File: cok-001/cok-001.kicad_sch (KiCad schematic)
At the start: 282 parts, among them J2501 HDMI_A, J3209 ATA Power, J3221 ATA0 for BD, J3301 USB_A_Stacked, J3302 USB_A_Stacked, J3401 Conn_01x22_Pin, J4001 Conn_01x03_Pin, J4003 Conn_01x02_Pin, J4009 Conn_01x30_Socket, J4010 Conn_01x10_Socket, Q2401 DTC144E, Q2402 SI2303BDS, Q4014 DTC143ZUA, U1101 ADT7461A0002RMZR, U1201 Y0_XDR0, U1202 Y0_XDR1, U1301 Y1_XDR0, U1302 Y1_XDR1, U2101 ADT7461A0002RMZR, U2105 TC7WP3125FK, U2108 ICS651MLFT, U2402 L7809, U2403 L7805, U2407 MM1593DFBEG, U3302 BU9869W, U3802 K9F1G08U0A, U3803 K9F1G08U0A, U6005 NCP511SN33T1G, U6006 NCP511SN18T1, U6008 NCP511SN18T1, U6009 NCP511SN33T1G, U6011 NCP511SN18T1, U6019 NCP511SN18T1, U7301 CXD9208GP, Y2101 24.576MHz, Y4001 Crystal, Y4002 Crystal

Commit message: sheets
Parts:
- removed C1103: 0.001u 50V, Capacitor_SMD:C_0402_1005Metric, symbol Device:C
- removed C1104, C1313, C1314, C1315, C1316, C1317, C1318, C1319, C1320, C1321, C1322, C1323, C1324, C1325, C1326, C1327, C1328, C1329, C1330, C1331, C1332, C1333, C1334, C1335, C1336, C1337, C1338, C1339, C1340, C1341, C1342: 0.1u 10V, Capacitor_SMD:C_0402_1005Metric, symbol Device:C
- removed R1106, R1107: 100, Resistor_SMD:R_0402_1005Metric, symbol Device:R_US
- removed U1101: ADT7461A0002RMZR, Package_SO:MSOP-8_3x3mm_P0.65mm, symbol PS3:ADT7461A
- removed U1201: Y0_XDR0, PS3:FBGA-104_16x11_15.18x14.56mm, symbol PS3:XDR_DRAM
- removed U1202: Y0_XDR1, PS3:FBGA-104_16x11_15.18x14.56mm, symbol PS3:XDR_DRAM
- removed U1301: Y1_XDR0, PS3:FBGA-104_16x11_15.18x14.56mm, symbol PS3:XDR_DRAM
- removed U1302: Y1_XDR1, PS3:FBGA-104_16x11_15.18x14.56mm, symbol PS3:XDR_DRAM
- added C2272: 100p, Capacitor_SMD:C_0402_1005Metric, symbol Device:C
- added C3314: 0.1u, Capacitor_SMD:C_0402_1005Metric, symbol Device:C
- added C3412, C3413, C3414, C3415: 0.01u, Capacitor_SMD:C_0402_1005Metric, symbol Device:C
- added D251, D252, D253, D254, D255, D256, D257, D258: ESD5Zxx, Diode_SMD:D_SOD-923, symbol Diode:ESD5Zxx
- added L2501, L2502, L2503, L2504, L3301, L3302, L3401, L3402: L_Iron_Coupled_Small, Inductor_SMD:L_CommonModeChoke_Coilcraft_0805USB, symbol Device:L_Iron_Coupled_Small_1243
- added R2106: 10k, Resistor_SMD:R_0402_1005Metric, symbol Device:R_US
- added R3328, R3329: 0, Resistor_SMD:R_0603_1608Metric, symbol Device:R_US
- added R3360, R3361, R3362, R3363, R3364, R3365, R3366, R3367: 0, Resistor_SMD:R_0402_1005Metric, symbol Device:R_US
- added TP9505, TP9506, TP9507, TP9508, TP9509, TP9510, TP9511, TP9512, TP9520, TP9522, TP9527, TP9529: TestPoint, TestPoint:TestPoint_Pad_1.0x1.0mm, symbol Connector:TestPoint
- added U3303: ~, Package_SO:SOIC-8_3.9x4.9mm_P1.27mm, symbol PS3:BD6517F
- added U3401: ~, Package_QFP:LQFP-64_10x10mm_P0.5mm, symbol PS3:88SA8040C0
- TP40005, TP4001, TP4002, TP4003, TP4004, TP4005, TP4006, TP4007, TP4008, TP4009, TP4016, TP4020, TP4021, TP4022, TP4034, TP4035, TP4036, TP4040, TP4044, TP4046, TP4075, TP4080, TP4081, TP4082, TP4083, TP4089, TP4090, TP4093, TP4096, TP4097, TP4105, TP9401, TP9402: footprint (none) -> TestPoint:TestPoint_Pad_1.0x1.0mm
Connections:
- net GND: now also U3305.1 (AGND), U3305.12 (ANGD), U3305.19 (AGND), U3305.23 (AGND), U3305.29 (AGND), C2272.2, C3314.2, D251.2 (A), D252.2 (A), D253.2 (A), D254.2 (A), D255.2 (A), D256.2 (A), D257.2 (A), D258.2 (A), U3303.6 (GND), U3401.42 (GND), U3401.57 (GND), U3401.8 (GND); no longer U2502.C1 (GND), U2502.C2
- net SW_AVCG: now also U2102.12 (OE), C2272.1, R2106.2
- net at U2102.6 (Vdd54): now also R2106.1
- net at J2501.1 (D2+): now also L2501.3
- net at J2501.10 (CK+): now also L2504.3
- net at J2501.12 (CK-): now also L2504.2
- net at J2501.19 (HPD): now also U2502.A1 (HPD)
- net at J2501.3 (D2-): now also L2501.2
- net at J2501.4 (D1+): now also L2502.3
- net at J2501.6 (D1-): now also L2502.2
- net at J2501.7 (D0+): now also L2503.3
- net at J2501.9 (D0-): now also L2503.2
- net at U4002.B16 (OSCOUT): now also C4028.1, Y4002.2
- net at U4002.C16 (OSCIN): now also C4027.1, Y4002.1
- net at J3302.1 (VBUS1): now also U3304.5 (OUTB), TP9522.1
- net at J3302.2 (D1-): now also L3301.4, TP9512.1
- net at J3302.3 (D1+): now also L3301.1, TP9511.1
- net at J3302.5 (VBUS2): now also U3304.8 (OUTA), TP9529.1
- net at J3302.6 (D2-): now also L3302.4, TP9510.1
- net at J3302.7 (D2+): now also L3302.1, TP9509.1
- net at U2502.A10 (TXC+_25): now also D252.1 (K), L2504.4
- net at U2502.A11 (TXC-_25): now also D251.1 (K), L2504.1
- net at U2502.A2 (TX2+_25): now also D258.1 (K), L2501.4
- net at U2502.A3 (TX2-_25): now also D257.1 (K), L2501.1
- net at U2502.A5 (TX1+_25): now also D256.1 (K), L2502.4
- net at U2502.A6 (TX1-_25): now also D255.1 (K), L2502.1
- net at U2502.A7 (TX0+_25): now also D254.1 (K), L2503.4
- net at U2502.A8 (TX0-_25): now also D253.1 (K), L2503.1
- net at U3305.14 (DM2): now also R3362.1
- net at U3305.15 (DP2): now also R3363.1
- net at U3305.25 (DM3): now also R3365.2
- net at U3305.26 (DP3): now also R3364.2
- net at U3305.3 (DM0): now also R3328.1
- net at U3305.31 (DM4): now also R3367.2
- net at U3305.32 (DP4): now also R3366.2
- net at U3305.4 (DP0): now also R3329.1
- net at U3305.8 (DM1): now also R3360.1
- net at U3305.9 (DP1): now also R3361.1
- net at J3301.1 (VBUS1): now also TP9520.1, U3303.5 (OUTB)
- net at J3301.2 (D1-): now also TP9508.1
- net at J3301.3 (D1+): now also TP9507.1
- net at J3301.5 (VBUS2): now also TP9527.1, U3303.8 (OUTA)
- net at J3301.6 (D2-): now also TP9506.1
- net at J3301.7 (D2+): now also TP9505.1
- net at J3401.S2 (A+): now also L3401.4
- net at J3401.S3 (A-): now also L3401.1
- net at J3401.S5 (B-): now also L3402.4
- net at J3401.S6 (B+): now also L3402.1
- new net: L3301.2, R3366.1
- new net: L3301.3, R3367.1
- new net: C3415.1, U3401.27 (RX_P)
- new net: C3415.2, L3402.2
- new net: C3413.1, U3401.28 (RX_M)
- new net: C3414.1, U3401.31 (TX_M)
- new net: C3412.1, U3401.32 (TX_P)
- new net: L3302.3, R3365.1
- new net: C3314.1, U3303.7 (VDD)
- new net: C3414.2, L3401.2
- new net: C3412.2, L3401.3
- new net: C3413.2, L3402.3
- new net: L3302.2, R3364.1
- new net SB_USB1_DM: R3328.2
- new net SB_USB1_DP: R3329.2
- no-connect marks 30 -> 37
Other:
- added sheet Resistors, Bypassing (resistors.kicad_sch)
- added sheet XDR DRAM (xdram.kicad_sch)
- moved on the sheet: C2101, C2102, C2451, C3246, C3247, C3301, C3309, C3311, C3313, C3316, C3328, C6116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

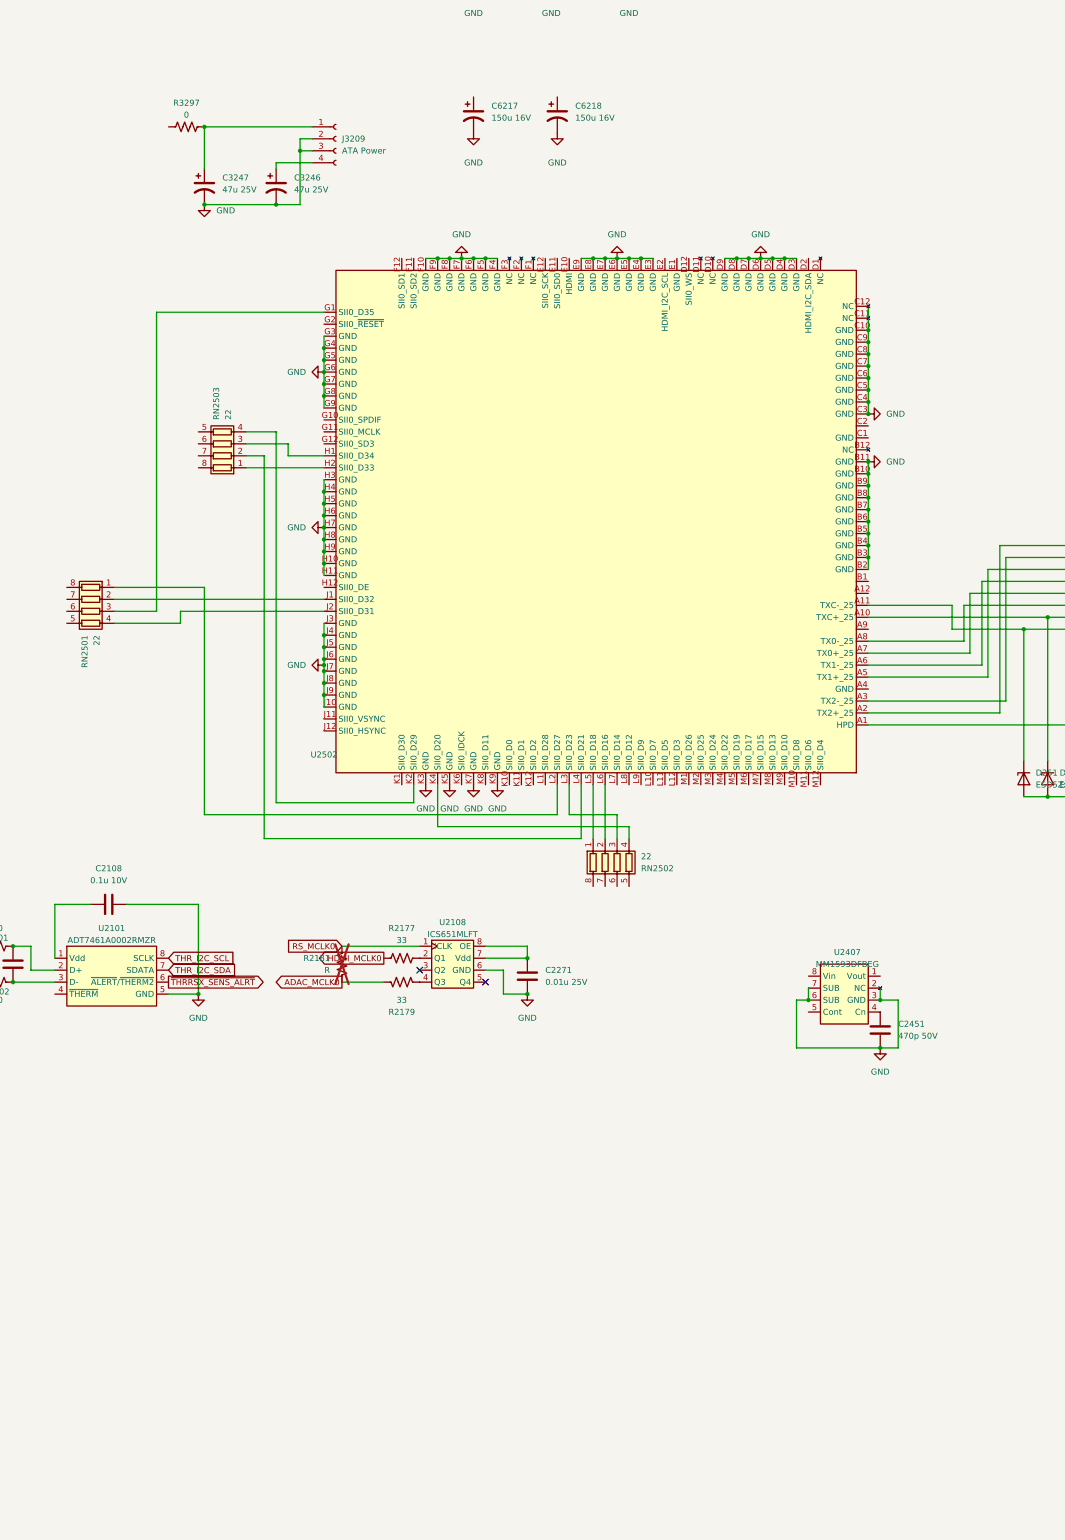
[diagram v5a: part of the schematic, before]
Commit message: fix Sil9132 symbol
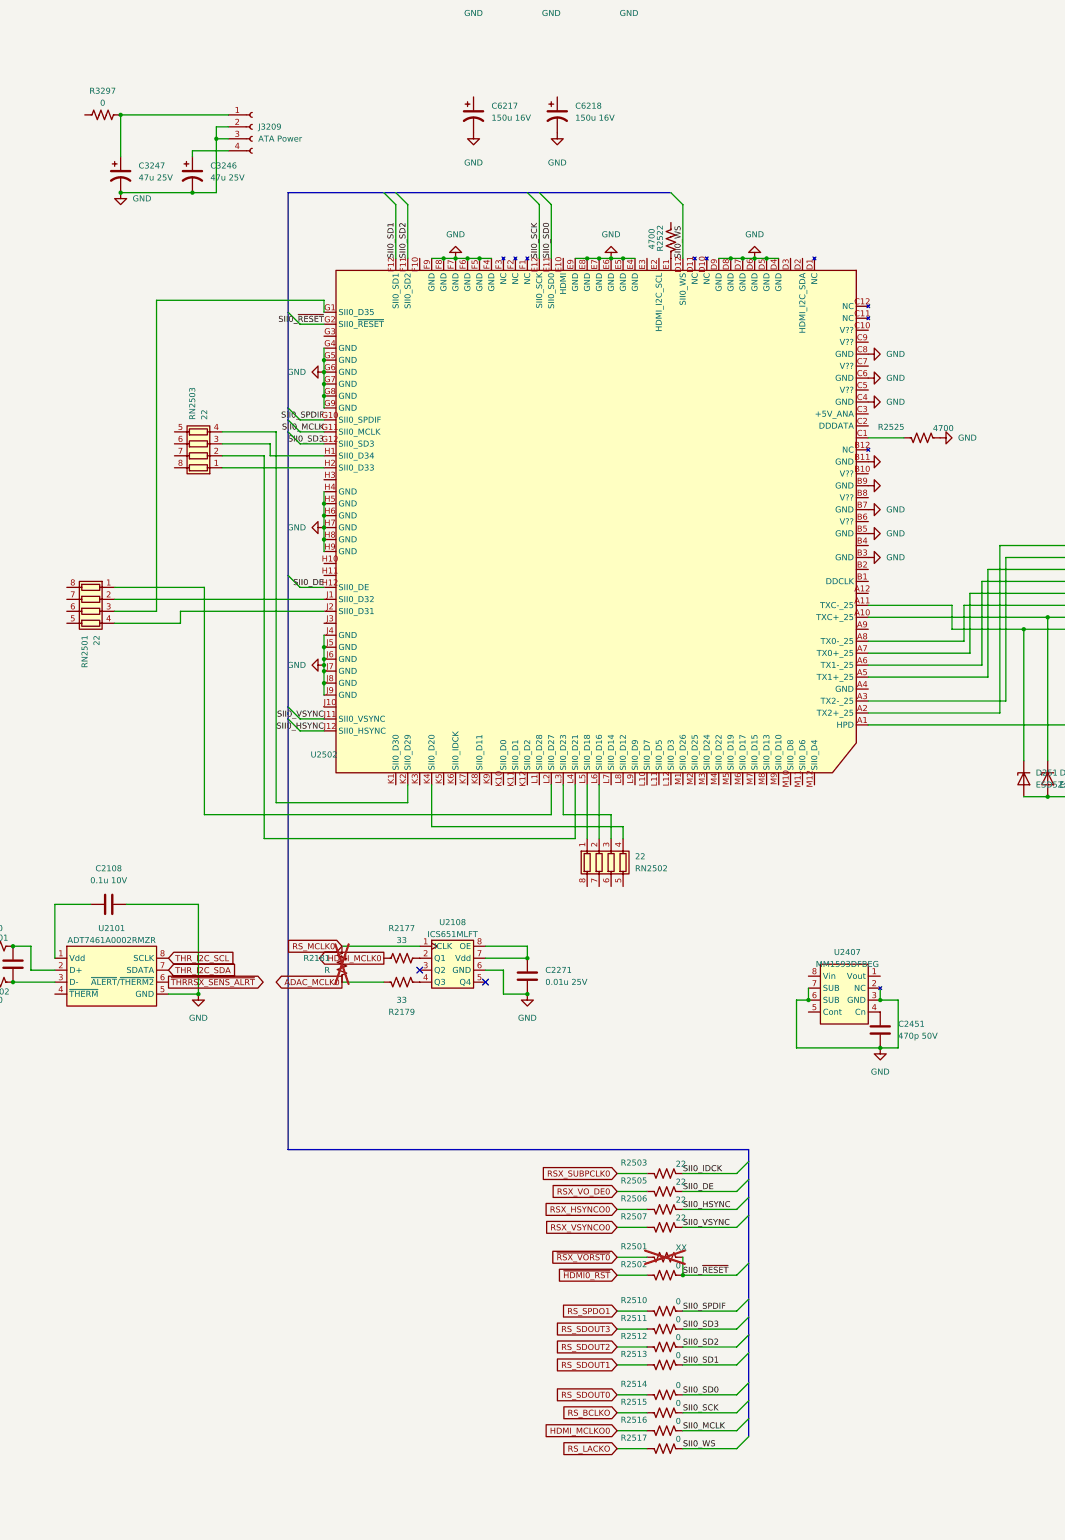
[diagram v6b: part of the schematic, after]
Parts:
- added R2501: XX, Resistor_SMD:R_0402_1005Metric, symbol Device:R_US
- added R2502, R2510, R2511, R2512, R2513, R2514, R2515, R2516, R2517: 0, Resistor_SMD:R_0402_1005Metric, symbol Device:R_US
- added R2503, R2505, R2506, R2507: 22, Resistor_SMD:R_0402_1005Metric, symbol Device:R_US
- added R2522, R2525: 4700, Resistor_SMD:R_0402_1005Metric, symbol Device:R_US
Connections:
- net GND: now also R2525.2; no longer U2502.B10 (GND), U2502.B2 (GND), U2502.B4 (GND), U2502.B6 (GND), U2502.B8 (GND), U2502.C10 (GND), U2502.C12 (NC), U2502.C3 (GND), U2502.C5 (GND), U2502.C7 (GND), U2502.C9 (GND), U2502.D3 (GND), U2502.E3 (GND), U2502.F10 (GND), U2502.G3 (GND), U2502.H10 (GND), U2502.H11 (GND), U2502.H3 (GND), U2502.J10 (GND), U2502.J3 (GND), U2502.K3 (GND), U2502.K5 (GND), U2502.K7 (GND), U2502.K9 (GND)
- net ~{HDMI0_RST}: now also R2502.1
- net at U4002.B16 (OSCOUT): now also C4028.1, Y4002.2
- net at U4002.C16 (OSCIN): now also C4027.1, Y4002.1
- net at U2502.C1: now also R2525.1
- net SII0_WS: now reaches U2502.D12 (SII0_WS)
- net SII0_WS: now also R2517.2
- net at U2502.E1: now also R2522.2
- net SII0_SD0: now reaches U2502.E11 (SII0_SD0)
- net SII0_SD0: now also R2514.2
- net SII0_SCK: now reaches U2502.E12 (SII0_SCK)
- net SII0_SCK: now also R2515.2
- net SII0_SD2: now reaches U2502.F11 (SII0_SD2)
- net SII0_SD2: now also R2512.2
- net SII0_SD1: now reaches U2502.F12 (SII0_SD1)
- net SII0_SD1: now also R2513.2
- net SII0_SPDIF: now reaches U2502.G10 (SII0_SPDIF)
- net SII0_SPDIF: now also R2510.2
- net SII0_MCLK: now reaches U2502.G11 (SII0_MCLK)
- net SII0_MCLK: now also R2516.2
- net SII0_SD3: now reaches U2502.G12 (SII0_SD3)
- net SII0_SD3: now also R2511.2
- net SII0_~{RESET}: now reaches U2502.G2 (SII0_~{RESET})
- net SII0_~{RESET}: now also R2501.2, R2502.2
- net SII0_DE: now reaches U2502.H12 (SII0_DE)
- net SII0_DE: now also R2505.2
- net SII0_VSYNC: now reaches U2502.J11 (SII0_VSYNC)
- net SII0_VSYNC: now also R2507.2
- net SII0_HSYNC: now reaches U2502.J12 (SII0_HSYNC)
- net SII0_HSYNC: now also R2506.2
- new net HDMI_MCLKO0: R2516.1
- new net RSX_HSYNCO0: R2506.1
- new net RSX_SUBPCLK0: R2503.1
- new net RSX_VO_DE0: R2505.1
- new net RSX_VSYNCO0: R2507.1
- new net RS_BCLKO: R2515.1
- new net RS_LACKO: R2517.1
- new net RS_SDOUT0: R2514.1
- new net RS_SDOUT1: R2513.1
- new net RS_SDOUT2: R2512.1
- new net RS_SDOUT3: R2511.1
- new net RS_SPDO1: R2510.1
- new net SII0_IDCK: R2503.2
- new net ~{RSX_VORST0}: R2501.1
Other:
- moved on the sheet: C3246, C3247, J3209, R3297, RN2502, RN2503

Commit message: added hdmi and jtag
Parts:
- removed D251, D252, D253, D254, D255, D256, D257, D258: ESD5Zxx, Diode_SMD:D_SOD-923, symbol Diode:ESD5Zxx
- removed J2501: HDMI_A, Connector_FFC-FPC:Hirose_FH12-19S-0.5SH_1x19-1MP_P0.50mm_Horizontal, symbol Connector:HDMI_A
- removed L2501, L2502, L2503, L2504: L_Iron_Coupled_Small, Inductor_SMD:L_CommonModeChoke_Coilcraft_0805USB, symbol Device:L_Iron_Coupled_Small_1243
- removed R2501: XX, Resistor_SMD:R_0402_1005Metric, symbol Device:R_US
- removed R2502, R2510, R2511, R2512, R2513, R2514, R2515, R2516, R2517: 0, Resistor_SMD:R_0402_1005Metric, symbol Device:R_US
- removed R2503, R2505, R2506, R2507: 22, Resistor_SMD:R_0402_1005Metric, symbol Device:R_US
- removed R2522, R2525: 4700, Resistor_SMD:R_0402_1005Metric, symbol Device:R_US
- removed RN2501, RN2502, RN2503: 22, Resistor_SMD:R_Array_Convex_4x0402, symbol Device:R_Pack04
- removed U2502: ~, Package_BGA:BGA-144_13.0x13.0mm_Layout12x12_P1.0mm, symbol PS3:Sil9132
- added H1, H2, H3, H4, H5, H6: MountingHole_Pad, MountingHole:MountingHole_4.3mm_M4_DIN965_Pad, symbol Mechanical:MountingHole_Pad
- D4007, D4008, D4009: footprint (none) -> Diode_SMD:D_SOD-923
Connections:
- net GND: now also H1.1, H2.1, H3.1, H4.1, H5.1, H6.1
- net at U4002.B16 (OSCOUT): now also C4028.1, Y4002.2
- net at U4002.C16 (OSCIN): now also C4027.1, Y4002.1
- no-connect marks 37 -> 35
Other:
- added sheet HDMI out (hdmi.kicad_sch)
- moved on the sheet: C2103, C2108, C2271, C2451, C3246, C3247, C6217, C6218, J3209, R2101, R2102, R2177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

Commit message: sif
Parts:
- removed C3823, C3824, C3825, C3826: 0.1u, Capacitor_SMD:C_0402_1005Metric, symbol Device:C
- removed C7347, C7348, C7349, C7350: 0.01u, Capacitor_SMD:C_0402_1005Metric, symbol Device:C
- removed C7354: 100p, Capacitor_SMD:C_0402_1005Metric, symbol Device:C
- removed R1, R7312, R7313: 56, Resistor_SMD:R_0402_1005Metric, symbol Device:R_US
- removed R3812, R3813, R3814, R3815: 0, Resistor_SMD:R_0402_1005Metric, symbol Device:R_US
- removed R3830, R3831, R3832, R3833, R3834, R3835, R3836, R3837: 10k, Resistor_SMD:R_0402_1005Metric, symbol Device:R_US
- removed R3840, R3841: 2200, Resistor_SMD:R_0402_1005Metric, symbol Device:R_US
- removed R7302, R7303, R7304, R7305, R7306, R7307, R7308, R7309: 4700, Resistor_SMD:R_0402_1005Metric, symbol Device:R_US
- removed R7314: 22, Resistor_SMD:R_0402_1005Metric, symbol Device:R_US
- removed RN7301, RN7302, RN7303, RN7304, RN7306, RN7307, RN7308, RN7309, RN7311: 56, Resistor_SMD:R_Array_Convex_4x0402, symbol Device:R_Pack04
- removed TP7301, TP7302, TP7303, TP7304, TP7305, TP7306, TP7307, TP7308, TP7309, TP7310, TP7311: TestPoint, TestPoint:TestPoint_Pad_1.0x1.0mm, symbol Connector:TestPoint
- removed U3801: ~, PS3:Starship2, symbol PS3:CXD43
- removed U3802, U3803: K9F1G08U0A, Package_SO:TSOP-I-48_18.4x12mm_P0.5mm, symbol PS3:K9F1G08
- removed U7301: CXD9208GP, Package_BGA:Xilinx_FTGB196, symbol PS3:CXD9208
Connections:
- net at U4002.B16 (OSCOUT): now also C4028.1, Y4002.2
- net at U4002.C16 (OSCIN): now also C4027.1, Y4002.1
- no-connect marks 35 -> 19
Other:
- added sheet PS2 Bridge (bridge.kicad_sch)
- added sheet Starship2 (starship.kicad_sch)
- moved on the sheet: U7002, U7003
